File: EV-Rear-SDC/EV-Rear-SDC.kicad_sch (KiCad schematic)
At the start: 47 parts, among them J1 JST-XA, J11 Conn_01x14, J2 JST-XA, J3 JST-XA, J4 JST-XA, J5 JST-XA, J6 JST-XA, J7 JST-XA, J8 Conn_01x03, K1 Relay_SPDT_G6RN, Q1 BSS205N, Q2 BSS205N, Q3 BSS205N, Q4 BSS205N, Q5 BSS205N, Q6 BSS205N, Q7 BSS205N, U2 MCP23S08-E_SS

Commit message: Add files via upload
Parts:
- added J10: IMU, CustomFootprints10:IMU, symbol Connector_Generic:Conn_01x10
- added J9: JST-XA, Custom_MSM:Connector_JST-XA_2POS, symbol Custom_MSM1:Connector_JST-XA_2POS
- R1, R18, R2, R3, R4, R5: value R -> 300
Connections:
- net +5V: now also J10.1 (Pin_1), J9.1 (Pin_1)
- net GND: now also J10.3 (Pin_3)
- net Inverter_low: now also J9.2 (Pin_2)
- net SCL: now reaches J11.7 (Pin_7)
- net SCL: now also J10.4 (Pin_4)
- net SDA: now reaches J11.8 (Pin_8)
- net SDA: now also J10.5 (Pin_5)
- no-connect marks 10 -> 11
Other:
- note added: "IMU"

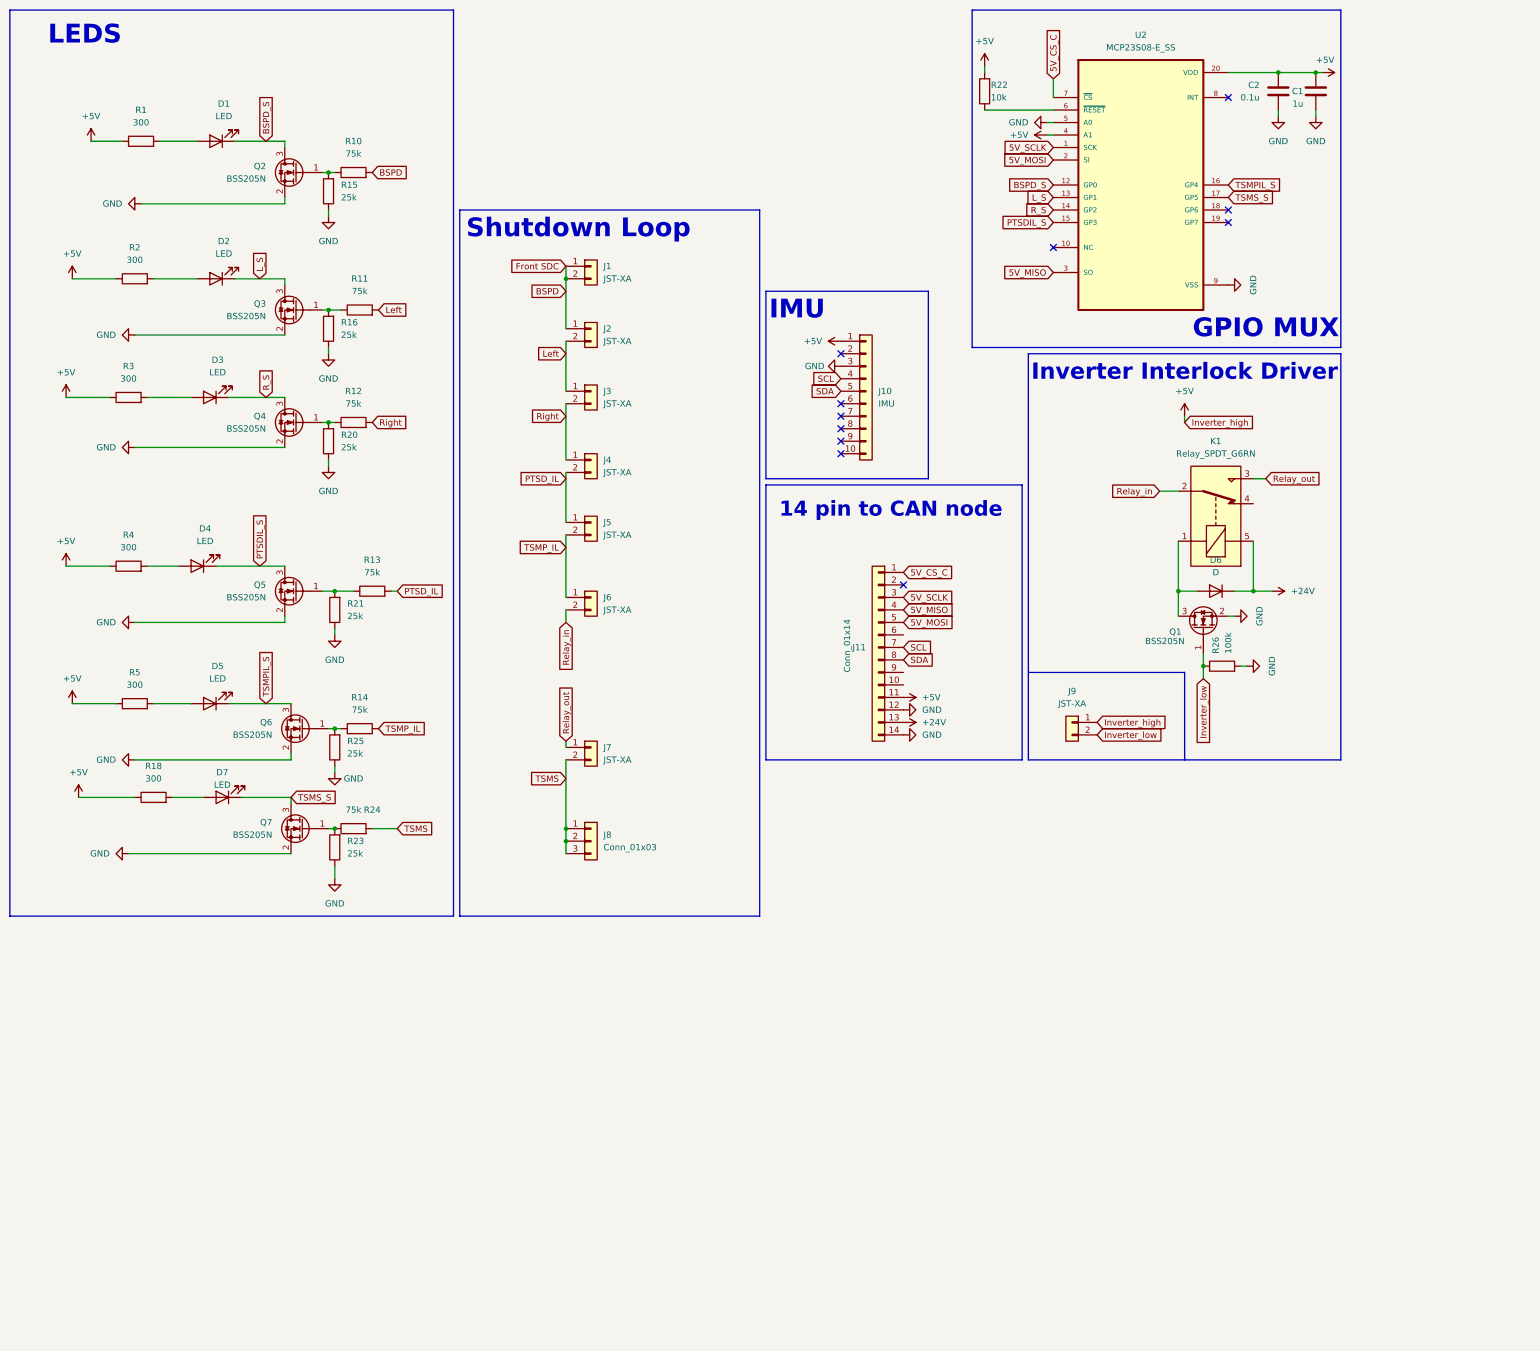
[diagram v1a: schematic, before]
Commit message: Added Level shifters for SPI
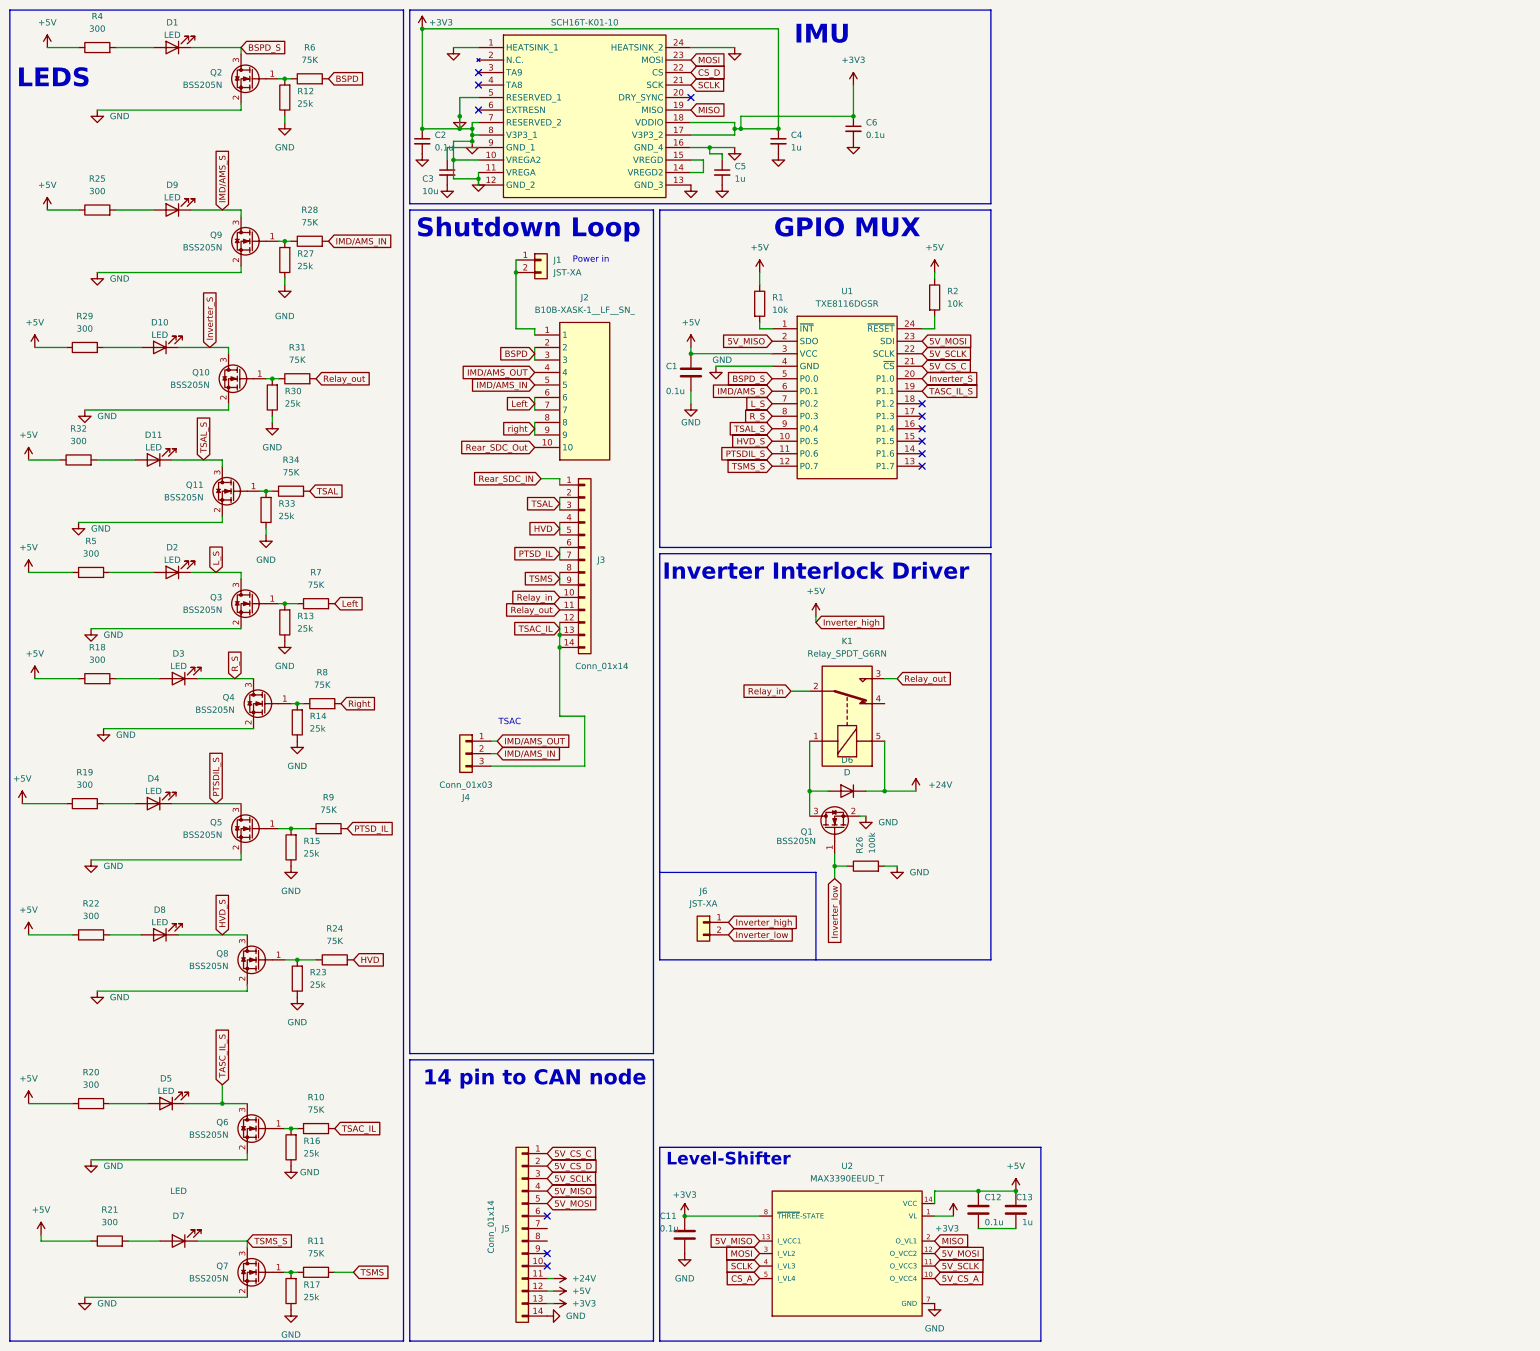
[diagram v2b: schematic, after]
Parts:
- removed C2: 0.1u, symbol Device:C
- removed J10: IMU, CustomFootprints10:IMU, symbol Connector_Generic:Conn_01x10
- removed J11: Conn_01x14, Connector_JST:JST_XA_S14B-XASK-1_1x14_P2.50mm_Horizontal, symbol Connector_Generic:Conn_01x14
- removed J2, J3, J4, J5, J6, J7: JST-XA, Custom_MSM:Connector_JST-XA_2POS, symbol Custom_MSM1:Connector_JST-XA_2POS
- removed J8: Conn_01x03, Connector_JST:JST_XA_S03B-XASK-1_1x03_P2.50mm_Horizontal, symbol Connector_Generic:Conn_01x03
- removed R3: 300, symbol Device:R
- removed U2: MCP23S08-E_SS, symbol MCP23S08-E_SS:MCP23S08-E_SS
- added C11, C12: 0.1u, Capacitor_SMD:C_0603_1608Metric, symbol Device:C
- added C13: 1u, Capacitor_SMD:C_0603_1608Metric, symbol Device:C
- added C2, C6: 0.1u, Capacitor_SMD:C_0603_1608Metric, symbol Device:C_Small
- added C3: 10u, Capacitor_SMD:C_0603_1608Metric, symbol Device:C_Small
- added C4, C5: 1u, Capacitor_SMD:C_0603_1608Metric, symbol Device:C_Small
- added D10, D11, D8, D9: LED, LED_SMD:LED_0603_1608Metric, symbol Device:LED
- added IC2: SCH16T-K01-10, Custom_MSM:SCH16TK0110, symbol SCH16T-K01-10:SCH16T-K01-10
- added J2: B10B-XASK-1__LF__SN_, Custom_MSM:B10BXASK1LFSN, symbol B10B-XASK-1__LF__SN_:B10B-XASK-1__LF__SN_
- added J3: Conn_01x14, Connector_JST:JST_XA_B14B-XASK-1_1x14_P2.50mm_Vertical, symbol Connector_Generic:Conn_01x14
- added J4: Conn_01x03, Connector_JST:JST_XA_S03B-XASK-1_1x03_P2.50mm_Horizontal, symbol Connector_Generic:Conn_01x03
- added J5: Conn_01x14, Custom_MSM:JST_XA_S14B-XASK-1_1x14_P2.50mm_Horizontal, symbol Connector_Generic:Conn_01x14
- added Q10, Q11, Q8, Q9: BSS205N, Custom_MSM:MOSFET_Single_SOT-23, symbol Custom_MSM1:MOSFET_N-CH
- added R17, R27, R30, R33: 25k, Resistor_SMD:R_0603_1608Metric, symbol Device:R
- added R19, R29, R32: 300, Resistor_SMD:R_0603_1608Metric, symbol Device:R
- added R28, R31, R34, R6, R7, R8, R9: 75K, Resistor_SMD:R_0603_1608Metric, symbol Device:R
- added U1: TXE8116DGSR, Custom_MSM:SOP50P490X110-24N, symbol Custom_MSM1:TXE8116DGSR
- added U2: MAX3390EEUD_T, customFootprints:SOP65P640X110-14N, symbol MAX3390EEUD_T:MAX3390EEUD_T
- C1: value 1u -> 0.1u; footprint (none) -> Capacitor_SMD:C_0603_1608Metric
- D1, D2, D3, D4, D5, D7: footprint (none) -> LED_SMD:LED_0603_1608Metric; MFN (none) -> LR Q976.01; S1PL (none) -> https://www.mouser.co.uk/en/ProductDetail/ams-OSRAM/LR-Q976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; S1PN (none) -> 720-LRQ976.01; S2PL (none) -> http://digikey.co.uk/en/products/detail/ams-osram-ag/LR-Q97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; S2PN (none) -> 475-LRQ976.01-P2R2-1CT-ND
- D6: footprint (none) -> Diode_SMD:D_0603_1608Metric
- J1: footprint Custom_MSM:Connector_JST-XA_2POS -> Custom_MSM:JST_XA_S02B-XASK-1_1x02_P2.50mm_Horizontal
- J6: renamed from J9; footprint Custom_MSM:Connector_JST-XA_2POS -> Custom_MSM:JST_XA_S02B-XASK-1_1x02_P2.50mm_Horizontal
- R1, R2: value 300 -> 10k; footprint (none) -> Resistor_SMD:R_0603_1608Metric
- R10, R11, R24: value 75k -> 75K; footprint (none) -> Resistor_SMD:R_0603_1608Metric; MFN (none) -> TNPW060375K0BHEA; S1PL (none) -> https://www.mouser.co.uk/en/ProductDetail/Vishay/TNPW060375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; S1PN (none) -> 71-TNPW060375K0BHEA; S2PL (none) -> https://www.digikey.co.uk/en/products/detail/vishay-dale/tn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; S2PN (none) -> 541-TNPW060375K0BHEACT-ND
- R12, R13, R14: value 75k -> 25k; footprint (none) -> Resistor_SMD:R_0603_1608Metric; MFN (none) -> PTN0603H2502BST1; S1PL (none) -> https://www.mouser.co.uk/en/ProductDetail/Vishay-Thin-Film/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; S1PN (none) -> Images are for reference only See Product Specifications Mo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
- R15, R16, R23: footprint (none) -> Resistor_SMD:R_0603_1608Metric; MFN (none) -> PTN0603H2502BST1; S1PL (none) -> https://www.mouser.co.uk/en/ProductDetail/Vishay-Thin-Film/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; S1PN (none) -> Images are for reference only See Product Specifications Mo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
- R18, R4, R5: footprint (none) -> Resistor_SMD:R_0603_1608Metric; MFN (none) -> CRCW0603300RJNEAHP; S1PL (none) -> https://www.mouser.co.uk/en/ProductDetail/Vishay/CRCW060330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; S1PN (none) -> 71-CRCW0603300RJNEAH; S2PL (none) -> https://www.digikey.co.uk/en/products/detail/vishay-dale/CR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; S2PN (none) -> 541-300SATR-ND
- R20, R21, R25: value 25k -> 300; footprint (none) -> Resistor_SMD:R_0603_1608Metric; MFN (none) -> CRCW0603300RJNEAHP; S1PL (none) -> https://www.mouser.co.uk/en/ProductDetail/Vishay/CRCW060330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; S1PN (none) -> 71-CRCW0603300RJNEAH; S2PL (none) -> https://www.digikey.co.uk/en/products/detail/vishay-dale/CR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; S2PN (none) -> 541-300SATR-ND
- R22: value 10k -> 300; footprint (none) -> Resistor_SMD:R_0603_1608Metric; MFN (none) -> CRCW0603300RJNEAHP; S1PL (none) -> https://www.mouser.co.uk/en/ProductDetail/Vishay/CRCW060330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; S1PN (none) -> 71-CRCW0603300RJNEAH; S2PL (none) -> https://www.digikey.co.uk/en/products/detail/vishay-dale/CR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; S2PN (none) -> 541-300SATR-ND
- R26: footprint (none) -> Resistor_SMD:R_0603_1608Metric
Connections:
- net +24V: now also J5.11 (Pin_11)
- net +5V: now also R20.1, R21.1, R22.1, R25.1, C12.1, C13.1, J5.12 (Pin_12), R19.1, R29.1, R32.1, U1.3 (VCC), U2.14 (VCC); no longer R22.2
- net 5V_CS_C: now also J5.1 (Pin_1), U1.21 (~{CS})
- net 5V_MISO: now also J5.4 (Pin_4), U1.2 (SDO), U2.13 (I_VCC1)
- net 5V_MOSI: now also J5.5 (Pin_5), U1.23 (SDI), U2.12 (O_VCC2)
- net 5V_SCLK: now also J5.3 (Pin_3), U1.22 (SCLK), U2.11 (O_VCC3)
- net BSPD: now also J2.2, J2.3, R6.2; no longer J1.1 (Pin_1), J1.2 (Pin_2), R10.2
- net BSPD_S: now also U1.5 (P0.0)
- net L_S: now also U1.7 (P0.2)
- net Left: now also J2.6, J2.7, R7.2; no longer R11.2
- net PTSDIL_S: now also U1.11 (P0.6)
- net PTSD_IL: now also J3.6 (Pin_6), J3.7 (Pin_7), R9.2; no longer R13.2
- net R_S: now also U1.8 (P0.3)
- net Relay_in: now also J3.10 (Pin_10)
- net Relay_out: now also J3.11 (Pin_11), R31.2
- net Right: now also R8.2; no longer R12.2
- net TSMS: now also R11.2, J3.8 (Pin_8), J3.9 (Pin_9); no longer R24.2
- net TSMS_S: now also U1.12 (P0.7)
- net at D4.2 (A): now also R19.2; no longer R4.2
- net at D1.2 (A): now also R4.2; no longer R1.2
- net at D3.2 (A): now also R18.2
- net at R5.2: now also D2.2 (A); no longer D5.2 (A)
- net at R2.2: now also U1.24 (~{RESET}); no longer D2.2 (A)
- net at R23.2, R24.1: now also Q8.1 (G); no longer Q7.1 (G)
- net at D7.2 (A): now also R21.2; no longer R18.2
- net GND renamed +3V3
- net +3V3: now also R12.1, R13.1, R14.1, C11.1, C11.2, C2.1, C2.2, C3.2, C4.1, C4.2, C5.1, C5.2, C6.1, C6.2, IC2.1 (HEATSINK_1), IC2.10 (VREGA2), IC2.11 (VREGA), IC2.12 (GND_2), IC2.13 (GND_3), IC2.16 (GND_4), IC2.17 (V3P3_2), IC2.18 (VDDIO), IC2.24 (HEATSINK_2), IC2.5 (RESERVED_1), IC2.7 (RESERVED_2), IC2.8 (V3P3_1), J5.13 (Pin_13), J5.14 (Pin_14), Q10.2 (S), Q11.2 (S), Q8.2 (S), Q9.2 (S), R17.1, R27.1, R30.1, R33.1, U1.4 (GND), U2.1 (VL), U2.7 (GND), U2.8 (~{THREE}-STATE); no longer R20.1, R21.1, R25.1
- net TSMPIL_S renamed TASC_IL_S
- net TASC_IL_S: now also U1.19 (P1.1)
- net TSMP_IL: no longer names the net of R14.2
- net TSMP_IL: now also Q4.1 (G), R8.1
- new net: Q2.1 (G), R12.2, R6.1
- new net: D10.2 (A), R29.2
- new net: Q5.1 (G), R15.2, R9.1
- new net: Q7.1 (G), R11.1, R17.2
- new net: Q9.1 (G), R27.2, R28.1
- new net: Q3.1 (G), R13.2, R7.1
- new net: Q6.1 (G), R10.1, R16.2
- new net: C3.1, IC2.9 (GND_1)
- new net: D11.2 (A), R32.2
- new net: Q10.1 (G), R30.2, R31.1
- new net: J1.1 (Pin_1), J1.2 (Pin_2), J2.1
- new net: C12.2, C13.2
- new net: Q11.1 (G), R33.2, R34.1
- new net: D8.2 (A), R22.2
- new net: D9.2 (A), R25.2
- new net: D5.2 (A), R20.2
- new net: IC2.14 (VREGD2), IC2.15 (VREGD)
- new net: R1.2, U1.1 (~{INT})
- new net 5V_CS_A: U2.10 (O_VCC4)
- new net 5V_CS_D: J5.2 (Pin_2)
- new net CS_A: U2.5 (I_VL4)
- new net CS_D: IC2.22 (CS)
- new net HVD: J3.4 (Pin_4), J3.5 (Pin_5), R24.2
- new net HVD_S: D8.1 (K), Q8.3 (D), U1.10 (P0.5)
- new net IMD/AMS_OUT: J2.4, J4.1 (Pin_1)
- new net IMD/AMS_S: D9.1 (K), Q9.3 (D), U1.6 (P0.1)
- new net IMD/AMS_IN: J2.5, J4.2 (Pin_2), R28.2
- new net Inverter_S: D10.1 (K), Q10.3 (D), U1.20 (P1.0)
- new net MISO: IC2.19 (MISO), U2.2 (O_VL1)
- new net MOSI: IC2.23 (MOSI), U2.3 (I_VL2)
- new net Rear_SDC_IN: J3.1 (Pin_1)
- new net Rear_SDC_Out: J2.10
- new net SCLK: IC2.21 (SCK), U2.4 (I_VL3)
- new net TSAC_IL: J3.12 (Pin_12), J3.13 (Pin_13), J3.14 (Pin_14), J4.3 (Pin_3), R10.2
- new net TSAL: J3.2 (Pin_2), J3.3 (Pin_3), R34.2
- new net TSAL_S: D11.1 (K), Q11.3 (D), U1.9 (P0.4)
- new net right: J2.8, J2.9
- no-connect marks 11 -> 13
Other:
- note added: "Level-Shifter"
- note added: "Power in"
- note added: "TSAC"
- moved on the sheet: D6, J1, J6, K1, Q1, Q2, Q3, Q4, Q5, Q6, Q7, R26

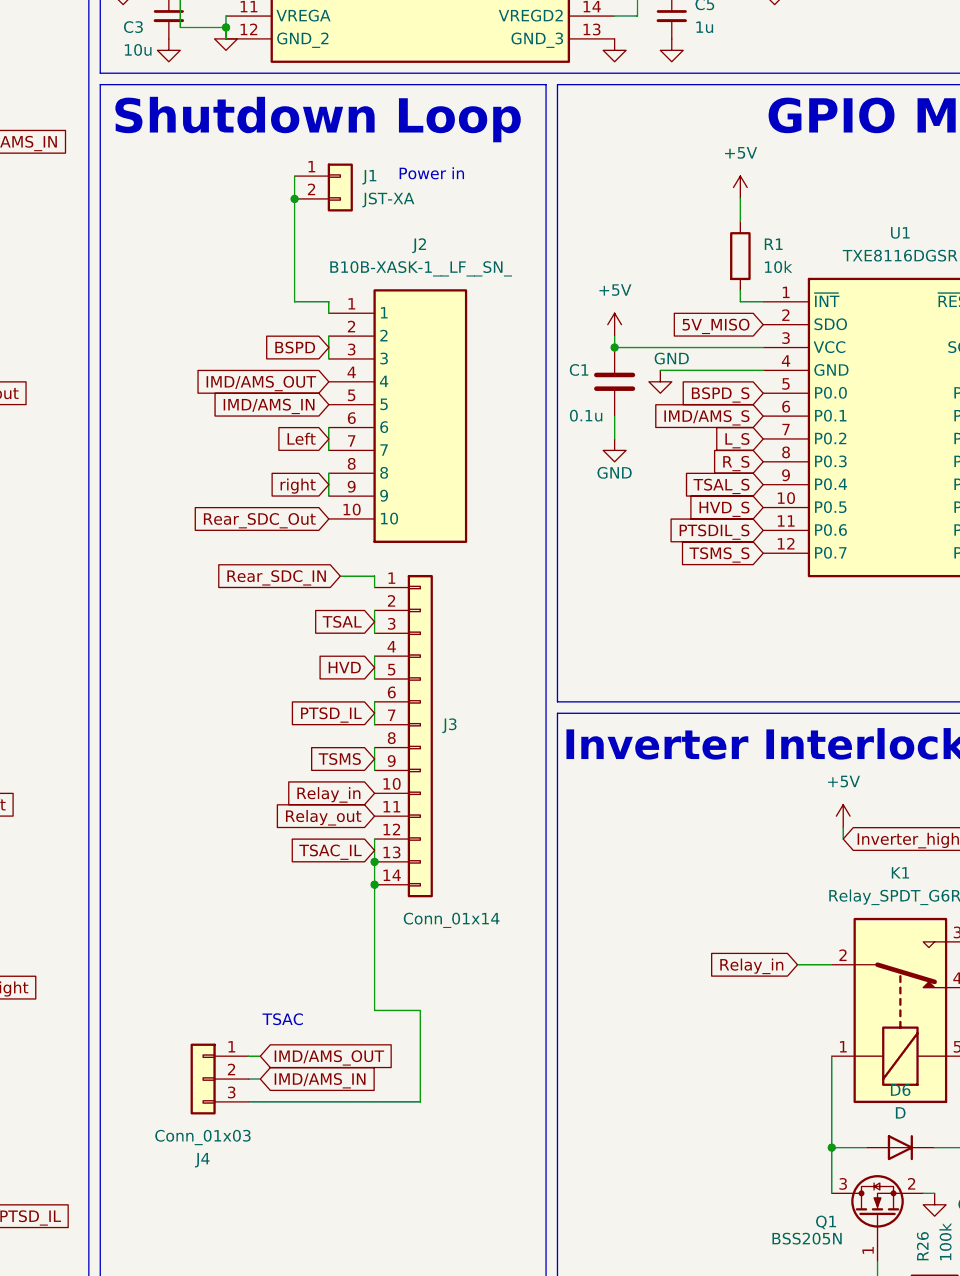
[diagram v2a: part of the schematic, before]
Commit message: Made changes to Rear SDC Routing
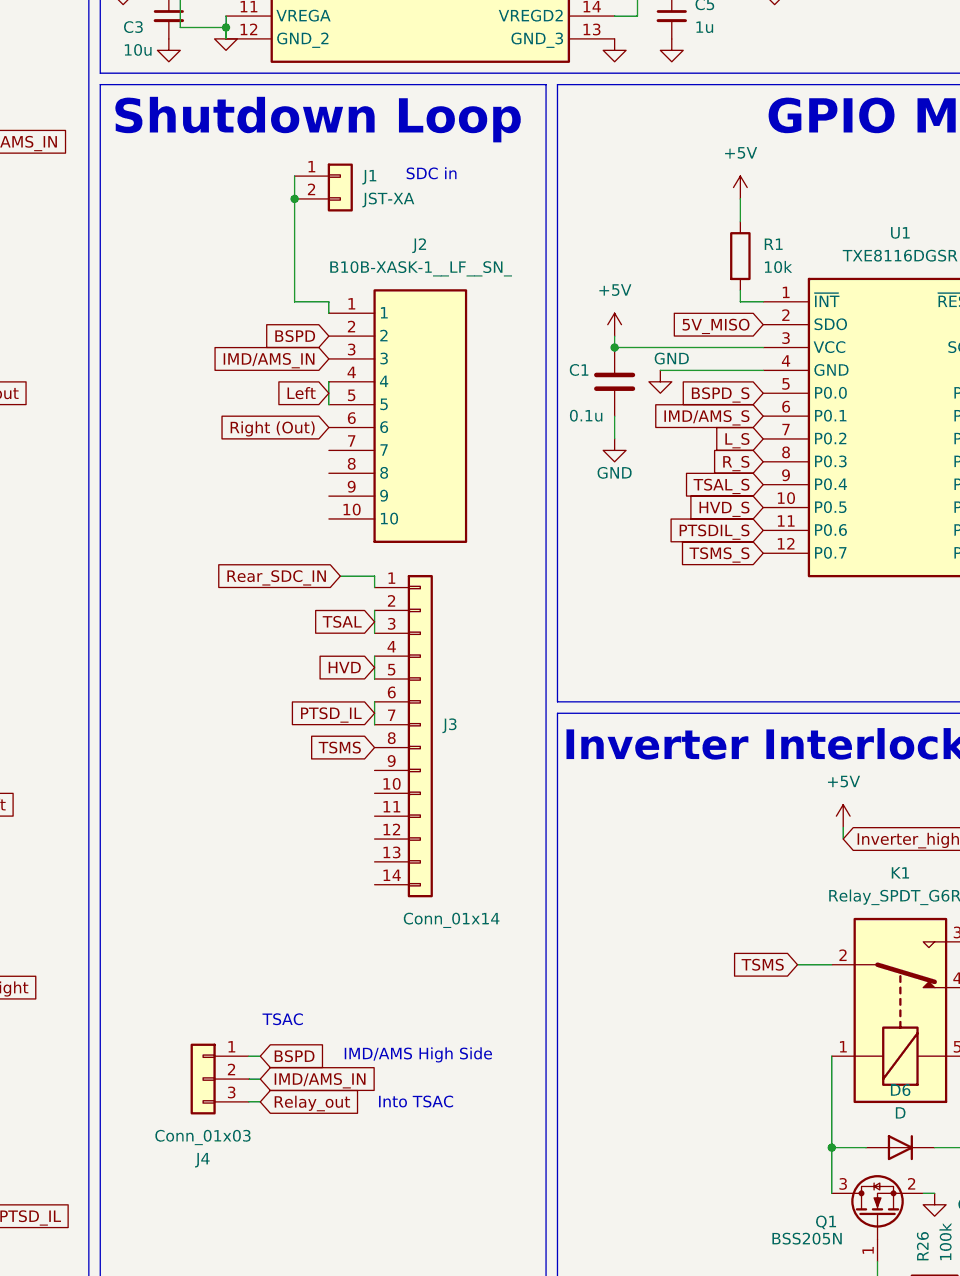
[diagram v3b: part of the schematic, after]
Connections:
- net BSPD: now also J4.1 (Pin_1); no longer J2.3
- net IMD/AMS_IN: now also J2.3; no longer J2.5
- net Left: now also J2.4, J2.5; no longer J2.6, J2.7
- net Relay_out: now also J4.3 (Pin_3); no longer J3.11 (Pin_11)
- net TSAC_IL: no longer J3.12 (Pin_12), J3.13 (Pin_13), J3.14 (Pin_14), J4.3 (Pin_3)
- net TSMS: now also K1.2; no longer J3.9 (Pin_9)
- removed net IMD/AMS_OUT: J2.4, J4.1 (Pin_1)
- net Rear_SDC_Out: no longer names the net of J2.10
- net Relay_in: no longer names the net of J3.10 (Pin_10)
- net Relay_in: no longer K1.2
- net right: no longer names the net of J2.8
- net right: no longer J2.9
- new net Right (Out): J2.6
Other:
- note added: "IMD/AMS High Side"
- note added: "Into TSAC"
- note added: "SDC in"
- note removed: "Power in"
